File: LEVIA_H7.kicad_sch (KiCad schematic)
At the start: 8 parts, among them U3 USBLC6-2P6

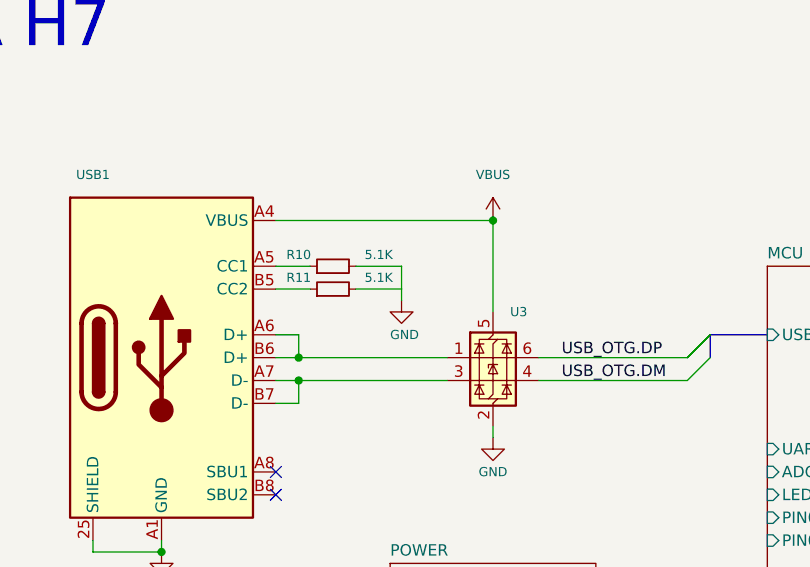
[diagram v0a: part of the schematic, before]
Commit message: grouped ICs and passives
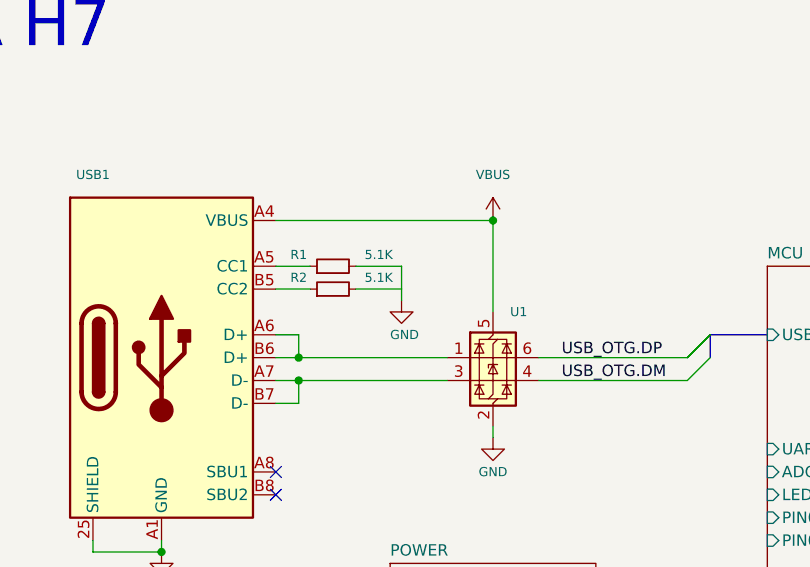
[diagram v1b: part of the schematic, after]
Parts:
- renumbered R10 to R1, R11 to R2, U3 to U1
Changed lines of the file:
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@@
 		(dnp no)
 		(fields_autoplaced yes)
-		(property "Reference" "#PWR0136"
+		(property "Reference" "#PWR07"
 			(at 121.92 182.88 0)
 			(hide yes)
@@
 			(project "LEVIA_H7"
 				(path "/6b768b36-fce6-4be0-9021-6d41bddc3a70"
-					(reference "#PWR0136")
+					(reference "#PWR07")
 					(unit 1)
 				)
@@
 		(dnp no)
 		(fields_autoplaced yes)
-		(property "Reference" "#PWR0123"
+		(property "Reference" "#PWR03"
 			(at 90.17 44.45 0)
 			(hide yes)
@@
 			(project "LEVIA_H7"
 				(path "/6b768b36-fce6-4be0-9021-6d41bddc3a70"
-					(reference "#PWR0123")
+					(reference "#PWR03")
 					(unit 1)
 				)
@@
 		(in_pos_files yes)
 		(dnp no)
-		(property "Reference" "#PWR024"
+		(property "Reference" "#PWR01"
 			(at 53.34 83.82 0)
 			(hide yes)
@@
 			(project "LEVIA_H7"
 				(path "/6b768b36-fce6-4be0-9021-6d41bddc3a70"
-					(reference "#PWR024")
+					(reference "#PWR01")
 					(unit 1)
 				)
@@
 		(in_pos_files yes)
 		(dnp no)
-		(property "Reference" "#PWR026"
+		(property "Reference" "#PWR02"
 			(at 80.01 55.88 0)
 			(hide yes)
@@
 			(project "LEVIA_H7"
 				(path "/6b768b36-fce6-4be0-9021-6d41bddc3a70"
-					(reference "#PWR026")
+					(reference "#PWR02")
 					(unit 1)
 				)
@@
 		(in_pos_files yes)
 		(dnp no)
-		(property "Reference" "R10"
+		(property "Reference" "R1"
 			(at 68.58 44.45 90)
 			(show_name no)
@@
 			(project "LEVIA_H7"
 				(path "/6b768b36-fce6-4be0-9021-6d41bddc3a70"
-					(reference "R10")
+					(reference "R1")
 					(unit 1)
 				)
@@
 		(in_pos_files yes)
 		(dnp no)
-		(property "Reference" "R11"
+		(property "Reference" "R2"
 			(at 68.58 46.99 90)
 			(show_name no)
@@
 			(project "LEVIA_H7"
 				(path "/6b768b36-fce6-4be0-9021-6d41bddc3a70"
-					(reference "R11")
+					(reference "R2")
 					(unit 1)
 				)
@@
 		(dnp no)
 		(fields_autoplaced yes)
-		(property "Reference" "#PWR0134"
+		(property "Reference" "#PWR05"
 			(at 106.68 182.88 0)
 			(hide yes)
@@
 			(project "LEVIA_H7"
 				(path "/6b768b36-fce6-4be0-9021-6d41bddc3a70"
-					(reference "#PWR0134")
+					(reference "#PWR05")
 					(unit 1)
 				)
@@
 		(in_pos_files yes)
 		(dnp no)
-		(property "Reference" "#PWR025"
+		(property "Reference" "#PWR04"
 			(at 90.17 71.12 0)
 			(hide yes)
@@
 			(project "LEVIA_H7"
 				(path "/6b768b36-fce6-4be0-9021-6d41bddc3a70"
-					(reference "#PWR025")
+					(reference "#PWR04")
 					(unit 1)
 				)
@@
 		(dnp no)
 		(fields_autoplaced yes)
-		(property "Reference" "#PWR0135"
+		(property "Reference" "#PWR06"
 			(at 114.3 182.88 0)
 			(hide yes)
@@
 			(project "LEVIA_H7"
 				(path "/6b768b36-fce6-4be0-9021-6d41bddc3a70"
-					(reference "#PWR0135")
+					(reference "#PWR06")
 					(unit 1)
 				)
@@
 		(dnp no)
 		(fields_autoplaced yes)
-		(property "Reference" "#PWR0137"
+		(property "Reference" "#PWR08"
 			(at 129.54 182.88 0)
 			(hide yes)
@@
 			(project "LEVIA_H7"
 				(path "/6b768b36-fce6-4be0-9021-6d41bddc3a70"
-					(reference "#PWR0137")
+					(reference "#PWR08")
 					(unit 1)
 				)
@@
 		(in_pos_files yes)
 		(dnp no)
-		(property "Reference" "U3"
+		(property "Reference" "U1"
 			(at 93.98 50.8 0)
 			(show_name no)
@@
 			(project "LEVIA_H7"
 				(path "/6b768b36-fce6-4be0-9021-6d41bddc3a70"
-					(reference "U3")
-					(unit 1)
-				)
+					(reference "U1")
+					(unit 1)
+				)

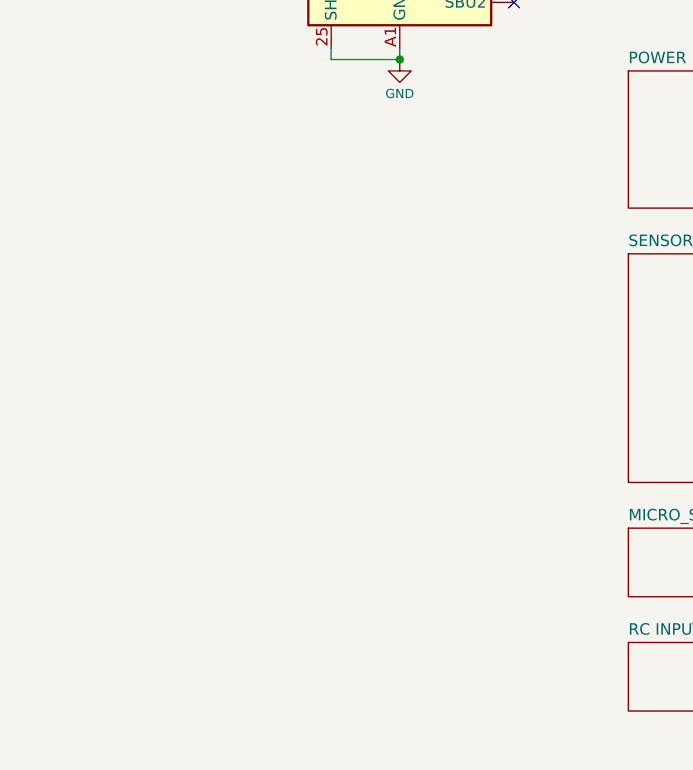
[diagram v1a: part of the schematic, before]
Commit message: defined stackup
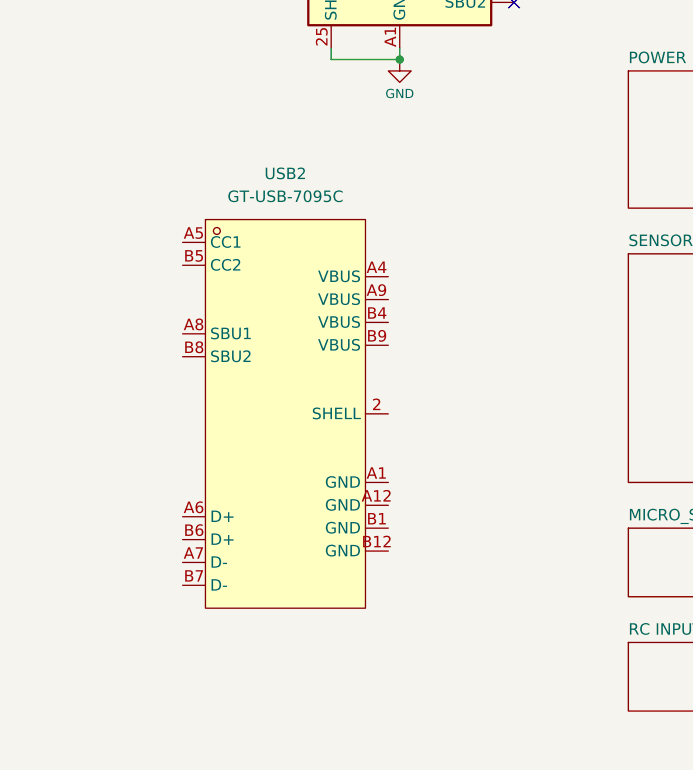
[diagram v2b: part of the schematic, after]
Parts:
- added USB2: GT-USB-7095C, EasyEDA:USB-C-SMD_GT-USB-7095C, symbol EasyEDA:GT-USB-7095C
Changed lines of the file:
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@@
+	)
+	(symbol
+		(lib_id "EasyEDA:GT-USB-7095C")
+		(at 41.91 116.84 0)
+		(unit 1)
+		(body_style 1)
+		(exclude_from_sim no)
+		(in_bom yes)
+		(on_board yes)
+		(in_pos_files yes)
+		(dnp no)
+		(fields_autoplaced yes)
+		(property "Reference" "USB2"
+			(at 40.64 90.17 0)
+			(show_name no)
+			(do_not_autoplace no)
+			(effects
+				(font
+					(size 1.27 1.27)
+				)
+			)
+		)
+		(property "Value" "GT-USB-7095C"
+			(at 40.64 92.71 0)
+			(show_name no)
+			(do_not_autoplace no)
+			(effects
+				(font
+					(size 1.27 1.27)
+				)
+			)
+		)
+		(property "Footprint" "EasyEDA:USB-C-SMD_GT-USB-7095C"
+			(at 41.91 143.51 0)
+			(hide yes)
+			(show_name no)
+			(do_not_autoplace no)
+			(effects
+				(font
+					(size 1.27 1.27)
+				)
+			)
+		)
+		(property "Datasheet" "https://www.lcsc.com/datasheet/C22387147.pdf"
+			(at 41.91 146.05 0)
+			(hide yes)
+			(show_name no)
+			(do_not_autoplace no)
+			(effects
+				(font
+					(size 1.27 1.27)
+				)
+			)
+		)
+		(property "Description" ""
+			(at 41.91 116.84 0)
+			(hide yes)
+			(show_name no)
+			(do_not_autoplace no)
+			(effects
+				(font
+					(size 1.27 1.27)
+				)
+			)
+		)
+		(property "Manufacturer" "G-Switch(品赞)"
+			(at 41.91 148.59 0)
+			(hide yes)
+			(show_name no)
+			(do_not_autoplace no)
+			(effects
+				(font
+					(size 1.27 1.27)
+				)
+			)
+		)
+		(property "MPN" "GT-USB-7095C"
+			(at 41.91 151.13 0)
+			(hide yes)
+			(show_name no)
+			(do_not_autoplace no)
+			(effects
+				(font
+					(size 1.27 1.27)
+				)
+			)
+		)
+		(property "LCSC Part" "C22387147"
+			(at 41.91 153.67 0)
+			(hide yes)
+			(show_name no)
+			(do_not_autoplace no)
+			(effects
+				(font
+					(size 1.27 1.27)
+				)
+			)
+		)
+		(pin "A4"
+		)
+		(pin "A1"
+		)
+		(pin "A5"
+		)
+		(pin "A8"
+		)
+		(pin "A7"
+		)
+		(pin "A6"
+		)
+		(pin "2"
+		)
+		(pin "B6"
+		)
+		(pin "B9"
+		)
+		(pin "B7"
+		)
+		(pin "B8"
+		)
+		(pin "B12"
+		)
+		(pin "B1"
+		)
+		(pin "B5"
+		)
+		(pin "B4"
+		)
+		(pin "A12"
+		)
+		(pin "A9"
+		)
+		(instances
+			(project "LEVIA_H7"
+				(path "/6b768b36-fce6-4be0-9021-6d41bddc3a70"
+					(reference "USB2")
+					(unit 1)
+				)
+			)
+		)
 	)
 	(symbol
